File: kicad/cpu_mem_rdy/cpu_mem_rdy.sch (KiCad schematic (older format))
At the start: 37 parts, among them CON1 USB-MICRO-B, P1 CONN_02X04, P3 CONN_01X03, P4 CONN_02X02, P6 POWER, SW1 SW_PUSH, U1 W65C02SP, U2 LM555N, U3 74HCT00, U4 74LS393, U6 28C256, U7 HM62256BLP-7, U8 HM62256BLP-7, X1 OSC

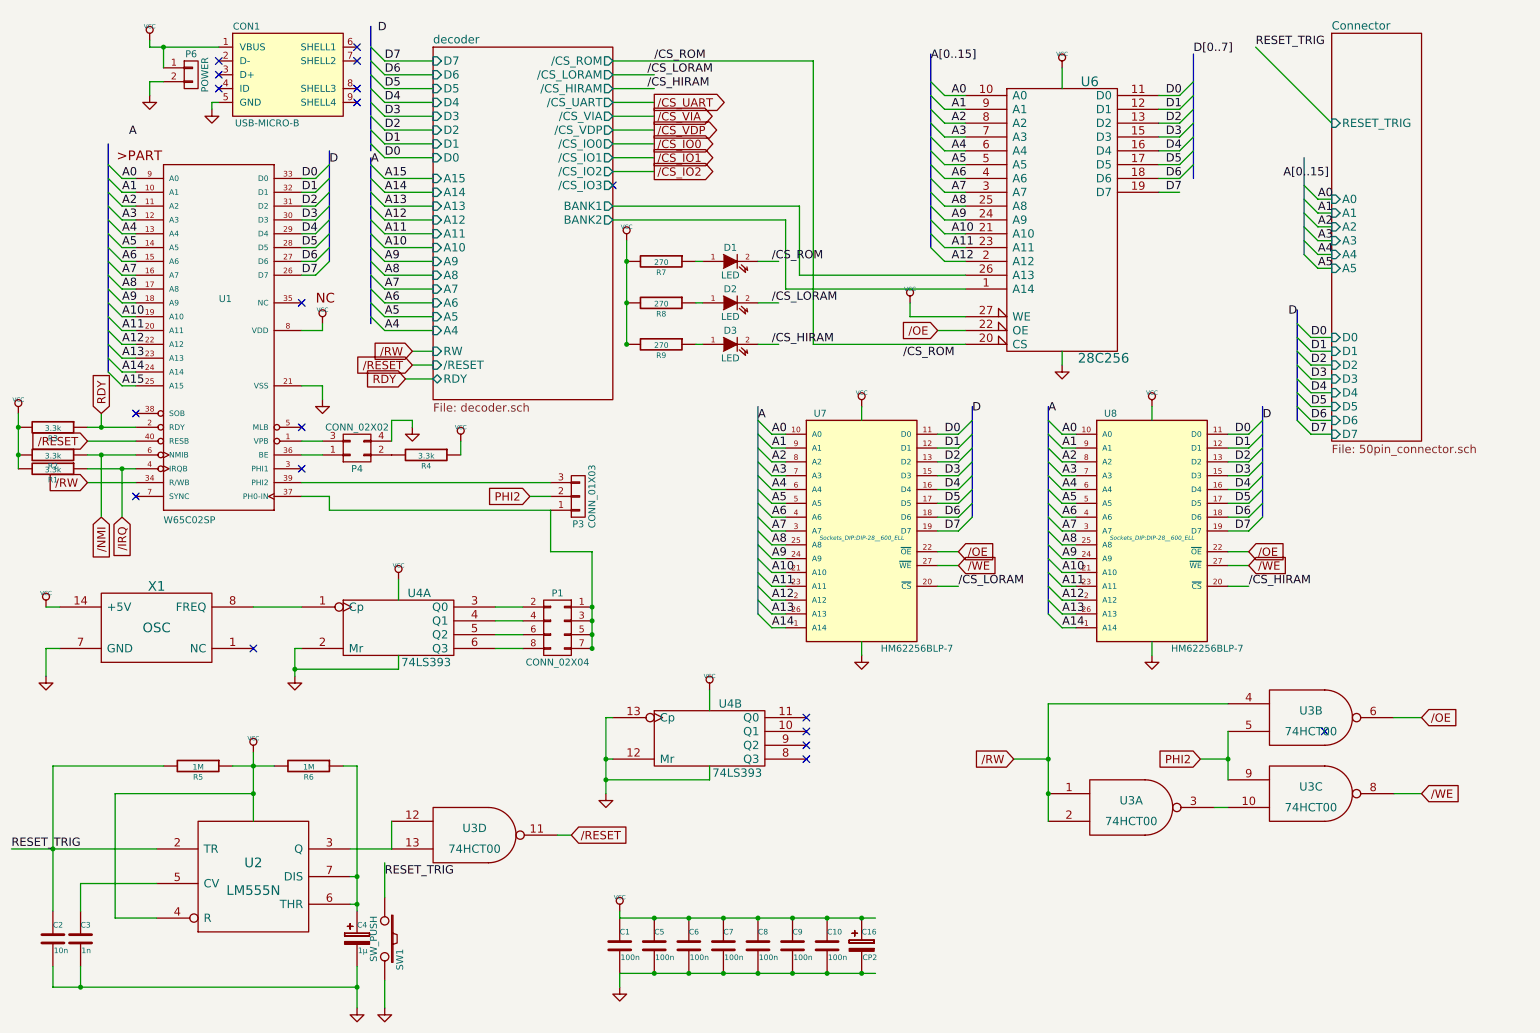
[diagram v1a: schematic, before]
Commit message: no rdy for via, io1-3 connected to rdygen
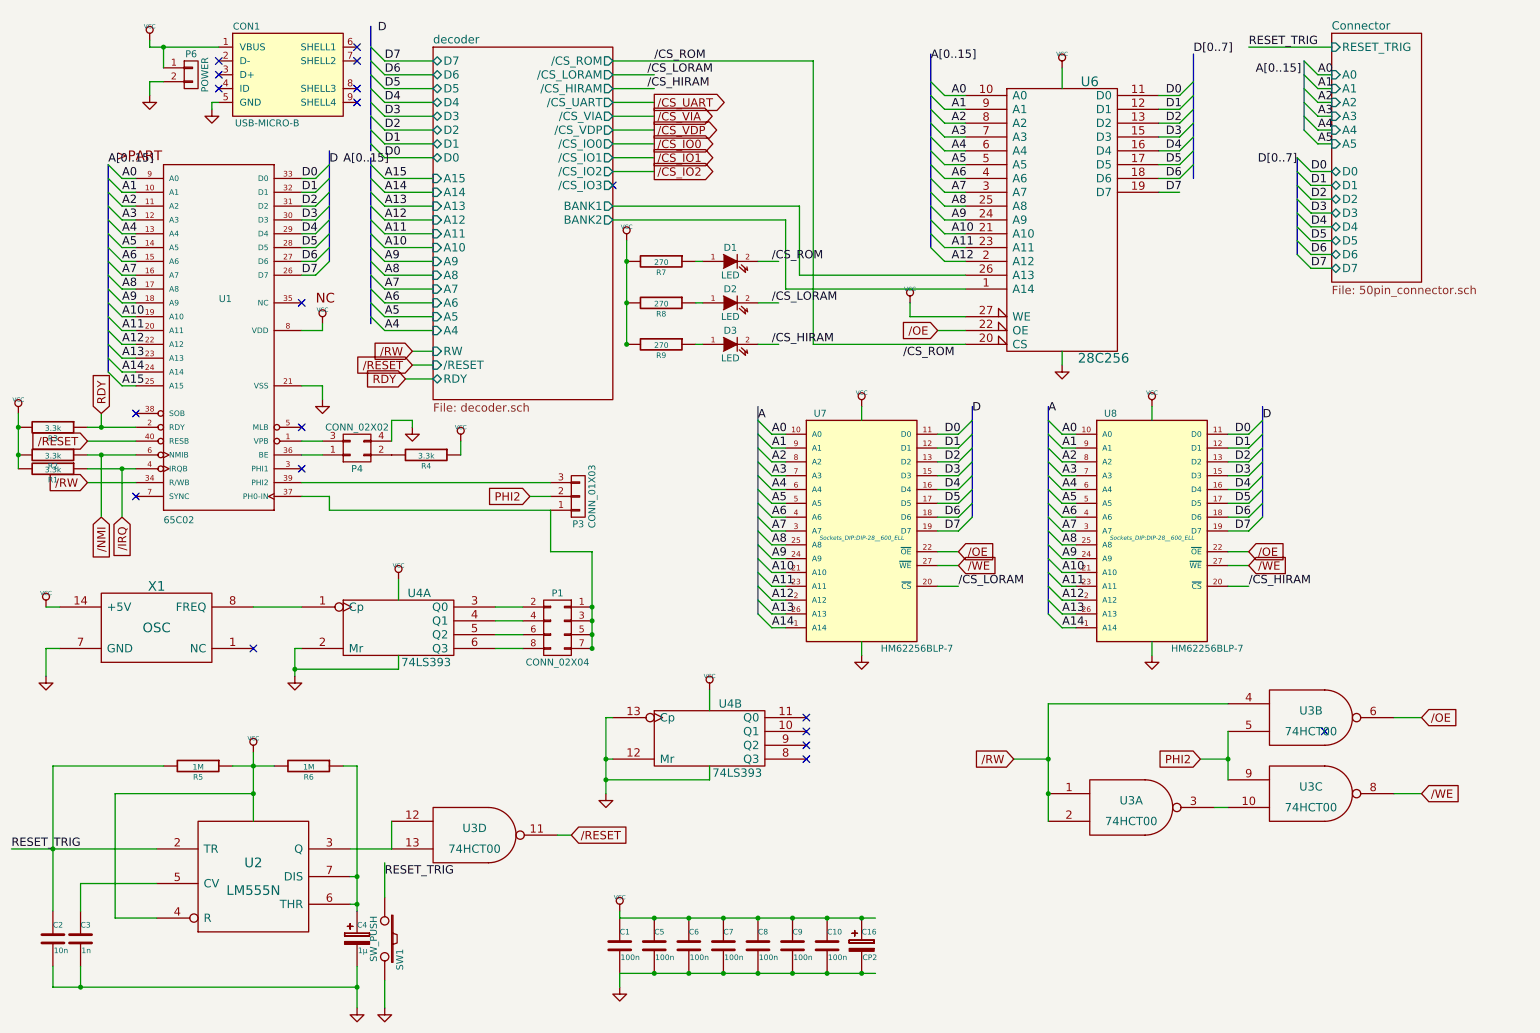
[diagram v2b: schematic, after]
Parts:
- U1: value W65C02SP -> 65C02; footprint Sockets_DIP:DIP-40__600_ELL -> Housings_DIP:DIP-40_W15.24mm_LongPads
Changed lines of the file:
@@
 P 2000 2550
 F 0 "U1" H 2000 2550 50  0000 L BNN
-F 1 "W65C02SP" H 1600 950 50  0000 L BNN
-F 2 "Sockets_DIP:DIP-40__600_ELL" H 2000 2700 50  0001 C CNN
+F 1 "65C02" H 1600 950 50  0000 L BNN
+F 2 "Housings_DIP:DIP-40_W15.24mm_LongPads" H 2000 2700 50  0001 C CNN
 F 3 "" H 2000 2550 60  0000 C CNN
 	1    2000 2550
@@
 Text Label 8000 3350 0    60   ~ 0
 A
-Text Label 1350 1350 0    60   ~ 0
-A
+Text Label 1200 1550 0    60   ~ 0
+A[0..15]
 Text Label 2800 1550 0    60   ~ 0
 D
@@
 $EndComp
 Entry Wire Line
-	9850 1700 9950 1800
-Text Label 9700 1650 0    60   ~ 0
+	9850 800  9950 900
+Text Label 9500 900  0    60   ~ 0
 A[0..15]
-Text Label 9950 1800 0    60   ~ 0
+Text Label 9950 900  0    60   ~ 0
 A0
 Entry Wire Line
-	9850 1800 9950 1900
-Entry Wire Line
-	9850 1900 9950 2000
-Entry Wire Line
-	9850 2000 9950 2100
-Entry Wire Line
-	9850 2100 9950 2200
-Text Label 9950 1900 0    60   ~ 0
+	9850 900  9950 1000
+Entry Wire Line
+	9850 1000 9950 1100
+Entry Wire Line
+	9850 1100 9950 1200
+Entry Wire Line
+	9850 1200 9950 1300
+Text Label 9950 1000 0    60   ~ 0
 A1
-Text Label 9950 2000 0    60   ~ 0
+Text Label 9950 1100 0    60   ~ 0
 A2
-Text Label 9950 2100 0    60   ~ 0
+Text Label 9950 1200 0    60   ~ 0
 A3
-Text Label 9950 2200 0    60   ~ 0
+Text Label 9950 1300 0    60   ~ 0
 A4
 Entry Wire Line
-	9900 2800 9800 2700
-Entry Wire Line
-	9900 2900 9800 2800
-Entry Wire Line
-	9900 3000 9800 2900
-Entry Wire Line
-	9900 3100 9800 3000
-Entry Wire Line
-	9900 3200 9800 3100
-Entry Wire Line
-	9900 3300 9800 3200
-Entry Wire Line
-	9900 3400 9800 3300
-Entry Wire Line
-	9900 3500 9800 3400
-Text Label 9800 2650 2    60   ~ 0
-D
+	9900 1600 9800 1500
+Entry Wire Line
+	9900 1700 9800 1600
+Entry Wire Line
+	9900 1800 9800 1700
+Entry Wire Line
+	9900 1900 9800 1800
+Entry Wire Line
+	9900 2000 9800 1900
+Entry Wire Line
+	9900 2100 9800 2000
+Entry Wire Line
+	9900 2200 9800 2100
+Entry Wire Line
+	9900 2300 9800 2200
+Text Label 9800 1550 2    60   ~ 0
+D[0..7]
 $Comp
 L 28C256 U6
@@
 	1    0    0    -1
 $EndComp
-Text Label 9900 2800 0    60   ~ 0
+Text Label 9900 1600 0    60   ~ 0
 D0
-Text Label 9900 2900 0    60   ~ 0
+Text Label 9900 1700 0    60   ~ 0
 D1
-Text Label 9900 3000 0    60   ~ 0
+Text Label 9900 1800 0    60   ~ 0
 D2
-Text Label 9900 3100 0    60   ~ 0
+Text Label 9900 1900 0    60   ~ 0
 D3
-Text Label 9900 3200 0    60   ~ 0
+Text Label 9900 2000 0    60   ~ 0
 D4
-Text Label 9900 3300 0    60   ~ 0
+Text Label 9900 2100 0    60   ~ 0
 D5
-Text Label 9900 3400 0    60   ~ 0
+Text Label 9900 2200 0    60   ~ 0
 D6
-Text Label 9900 3500 0    60   ~ 0
+Text Label 9900 2300 0    60   ~ 0
 D7
 Text GLabel 1150 4100 3    60   Input ~ 0
@@
 RDY
 Entry Wire Line
-	9850 2200 9950 2300
-Text Label 9950 2300 0    60   ~ 0
+	9850 1300 9950 1400
+Text Label 9950 1400 0    60   ~ 0
 A5
 $Comp
@@
 F1 "decoder.sch" 60
 F2 "A4" I L 3550 2750 60
-F3 "D0" I L 3550 1500 60
-F4 "D1" I L 3550 1400 60
-F5 "D2" I L 3550 1300 60
-F6 "D3" I L 3550 1200 60
-F7 "D4" I L 3550 1100 60
-F8 "D5" I L 3550 1000 60
-F9 "D6" I L 3550 900 60
-F10 "D7" I L 3550 800 60
+F3 "D0" B L 3550 1500 60
+F4 "D1" B L 3550 1400 60
+F5 "D2" B L 3550 1300 60
+F6 "D3" B L 3550 1200 60
+F7 "D4" B L 3550 1100 60
+F8 "D5" B L 3550 1000 60
+F9 "D6" B L 3550 900 60
+F10 "D7" B L 3550 800 60
 F11 "A5" I L 3550 2650 60
 F12 "A6" I L 3550 2550 60
@@
 	3100 1400 3200 1500
 Wire Bus Line
-	1200 1400 1200 3050
+	1200 1550 1200 3050
 Wire Bus Line
 	2800 1450 2800 2250
@@
 	1250 7000 1250 6100
 Wire Wire Line
-	1250 6100 2250 6100
+	2250 6100 1250 6100
 Connection ~ 2250 6100
 Wire Wire Line
@@
 	3400 3400 3400 3450
 Wire Bus Line
-	9850 1500 9850 2200
-Wire Wire Line
-	9950 1800 10050 1800
-Wire Wire Line
-	9950 1900 10050 1900
-Wire Wire Line
-	9950 2000 10050 2000
-Wire Wire Line
-	9950 2100 10050 2100
+	9850 800  9850 1300
+Wire Wire Line
+	9950 900  10050 900
+Wire Wire Line
+	9950 1000 10050 1000
+Wire Wire Line
+	9950 1100 10050 1100
+Wire Wire Line
+	9950 1200 10050 1200
 Wire Bus Line
-	9800 2600 9800 3400
-Wire Wire Line
-	9900 2800 10050 2800
-Wire Wire Line
-	10050 2900 9900 2900
-Wire Wire Line
-	9900 3000 10050 3000
-Wire Wire Line
-	10050 3100 9900 3100
-Wire Wire Line
-	9900 3200 10050 3200
-Wire Wire Line
-	10050 3300 9900 3300
-Wire Wire Line
-	9900 3400 10050 3400
-Wire Wire Line
-	10050 3500 9900 3500
+	9800 1500 9800 2200
+Wire Wire Line
+	9900 1600 10050 1600
+Wire Wire Line
+	10050 1700 9900 1700
+Wire Wire Line
+	9900 1800 10050 1800
+Wire Wire Line
+	10050 1900 9900 1900
+Wire Wire Line
+	9900 2000 10050 2000
+Wire Wire Line
+	10050 2100 9900 2100
+Wire Wire Line
+	9900 2200 10050 2200
+Wire Wire Line
+	10050 2300 9900 2300
 Wire Wire Line
 	1150 4100 1150 3650
@@
 Connection ~ 6650 7400
 Wire Wire Line
-	9950 2200 10050 2200
-Wire Wire Line
-	9950 2300 10050 2300
+	9950 1300 10050 1300
+Wire Wire Line
+	9950 1400 10050 1400
 Wire Wire Line
 	8100 3000 8100 2900
@@
 Wire Wire Line
 	3200 2750 3550 2750
-Text Label 3100 1550 0    60   ~ 0
-A
+Text Label 2900 1550 0    60   ~ 0
+A[0..15]
 Text Label 3200 1650 0    60   ~ 0
 A15
@@
 NoConn ~ 6250 5850
 Wire Wire Line
-	10050 1250 9500 700
-Text Label 9500 700  0    60   ~ 0
+	10050 700  9450 700
+Text Label 9450 700  0    60   ~ 0
 RESET_TRIG
 Text Label 500  6500 0    60   ~ 0
@@
 Wire Wire Line
 	3350 3100 3550 3100
-$Sheet
-S 10050 600  650  2950
-U 54206EE0
-F0 "Connector" 60
-F1 "50pin_connector.sch" 60
-F2 "A0" I L 10050 1800 60
-F3 "A1" I L 10050 1900 60
-F4 "A2" I L 10050 2000 60
-F5 "A3" I L 10050 2100 60
-F6 "A4" I L 10050 2200 60
-F7 "D0" I L 10050 2800 60
-F8 "D1" I L 10050 2900 60
-F9 "D2" I L 10050 3000 60
-F10 "D3" I L 10050 3100 60
-F11 "D4" I L 10050 3200 60
-F12 "D5" I L 10050 3300 60
-F13 "D6" I L 10050 3400 60
-F14 "D7" I L 10050 3500 60
-F15 "A5" I L 10050 2300 60
-F16 "RESET_TRIG" I L 10050 1250 60
-$EndSheet
 $Comp
 L USB-MICRO-B CON1
@@
 Wire Wire Line
 	1500 700  1500 650
+$Sheet
+S 10050 600  650  1800
+U 54206EE0
+F0 "Connector" 60
+F1 "50pin_connector.sch" 60
+F2 "A0" I L 10050 900 60
+F3 "A1" I L 10050 1000 60
+F4 "A2" I L 10050 1100 60
+F5 "A3" I L 10050 1200 60
+F6 "A4" I L 10050 1300 60
+F7 "D0" B L 10050 1600 60
+F8 "D1" B L 10050 1700 60
+F9 "D2" B L 10050 1800 60
+F10 "D3" B L 10050 1900 60
+F11 "D4" B L 10050 2000 60
+F12 "D5" B L 10050 2100 60
+F13 "D6" B L 10050 2200 60
+F14 "D7" B L 10050 2300 60
+F15 "A5" I L 10050 1400 60
+F16 "RESET_TRIG" I L 10050 700 60
+$EndSheet
 $EndSCHEMATC

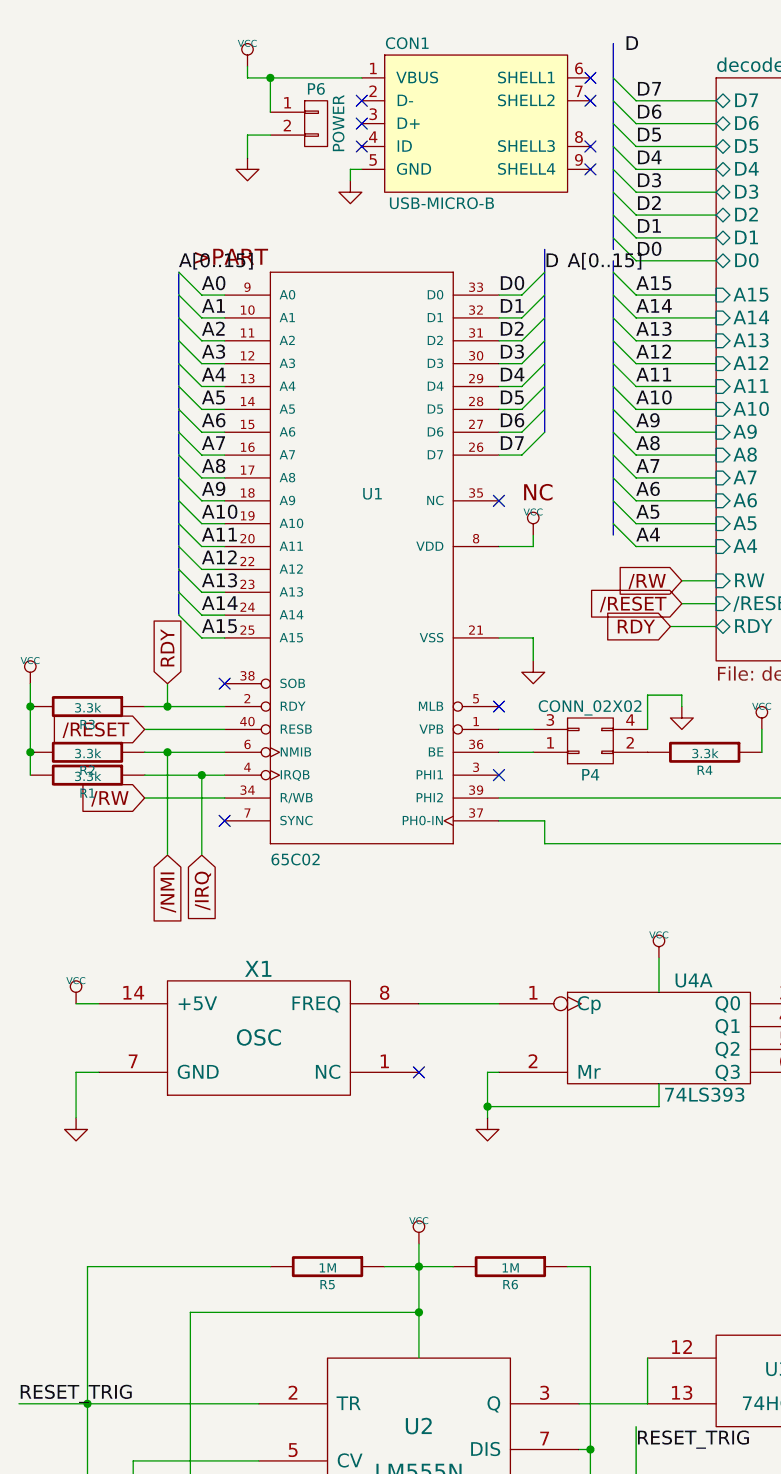
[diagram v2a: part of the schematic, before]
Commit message: USB B for power
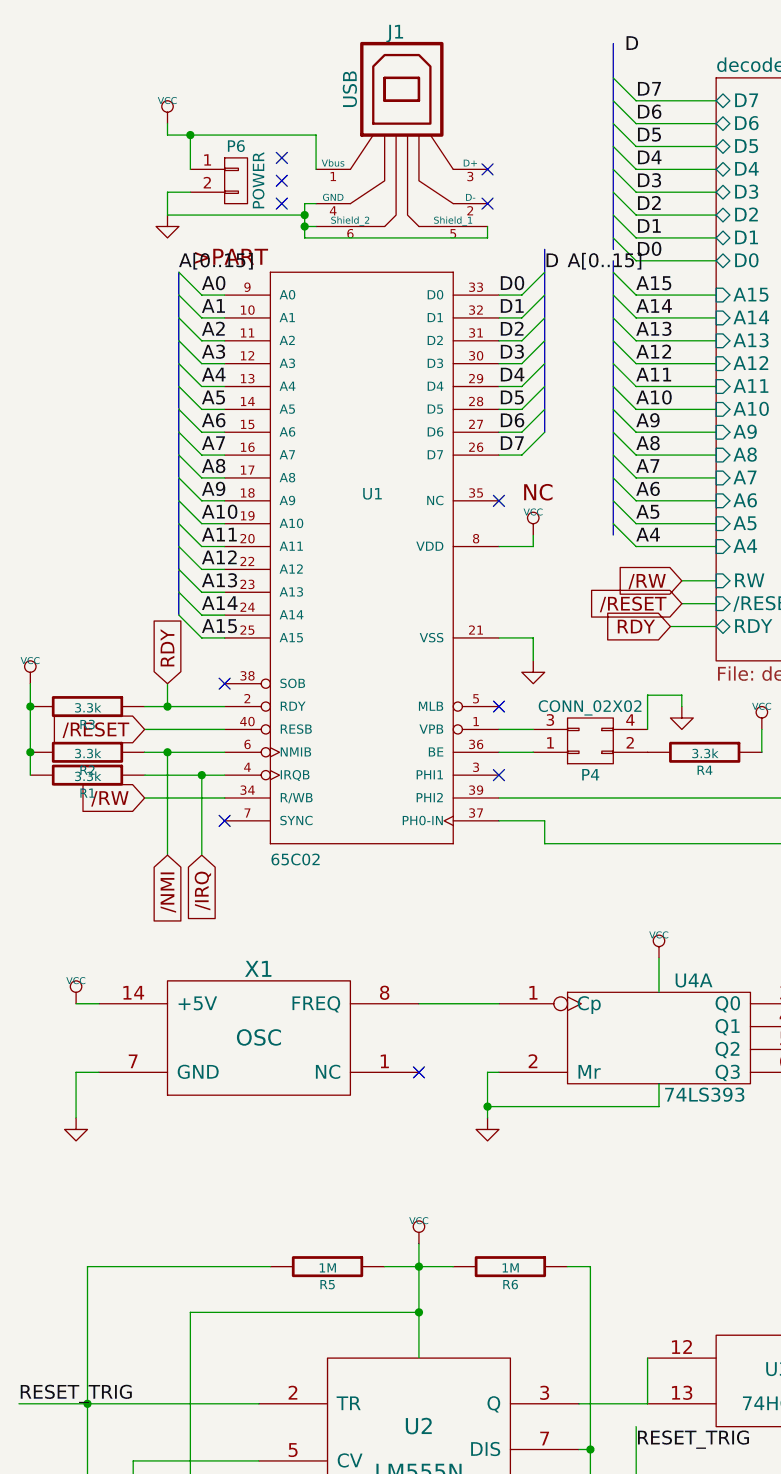
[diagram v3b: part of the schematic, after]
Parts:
- removed CON1: USB-MICRO-B, Connect:USB_Micro-B, symbol USB-MICRO-B
- added J1: USB, Connect:USB_B, symbol USB
- U1: footprint Housings_DIP:DIP-40_W15.24mm_LongPads -> Sockets_DIP:DIP-40__600_ELL
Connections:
- net GND: now also J1.4 (GND), J1.5 (Shield_1), J1.6 (Shield_2)
- net VCC: now also J1.1 (Vbus)
- no-connect marks 19 -> 17
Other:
- moved on the sheet: P6
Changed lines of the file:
@@
 F 0 "U1" H 2000 2550 50  0000 L BNN
 F 1 "65C02" H 1600 950 50  0000 L BNN
-F 2 "Housings_DIP:DIP-40_W15.24mm_LongPads" H 2000 2700 50  0001 C CNN
+F 2 "Sockets_DIP:DIP-40__600_ELL" H 2000 2700 50  0001 C CNN
 F 3 "" H 2000 2550 60  0000 C CNN
 	1    2000 2550
@@
 	1250 7000 1250 6100
 Wire Wire Line
-	2250 6100 1250 6100
+	1250 6100 2250 6100
 Connection ~ 2250 6100
 Wire Wire Line
@@
 L GND #PWR024
 U 1 1 54B5858D
-P 1500 1050
-F 0 "#PWR024" H 1500 1050 30  0001 C CNN
-F 1 "GND" H 1500 980 30  0001 C CNN
-F 2 "" H 1500 1050 60  0000 C CNN
-F 3 "" H 1500 1050 60  0000 C CNN
-	1    1500 1050
-	1    0    0    -1
-$EndComp
-Wire Wire Line
-	1600 950  1500 950
-Wire Wire Line
-	1500 950  1500 1050
+P 1150 1300
+F 0 "#PWR024" H 1150 1300 30  0001 C CNN
+F 1 "GND" H 1150 1230 30  0001 C CNN
+F 2 "" H 1150 1300 60  0000 C CNN
+F 3 "" H 1150 1300 60  0000 C CNN
+	1    1150 1300
+	1    0    0    -1
+$EndComp
+Wire Wire Line
+	1250 1200 1150 1200
+Wire Wire Line
+	1150 1200 1150 1300
 $Comp
 L LED D1
@@
 Wire Wire Line
 	3350 3100 3550 3100
-$Comp
-L USB-MICRO-B CON1
-U 1 1 56B0E071
-P 2500 900
-F 0 "CON1" H 2200 1250 50  0000 C CNN
-F 1 "USB-MICRO-B" H 2350 550 50  0000 C CNN
-F 2 "Connect:USB_Micro-B" H 2500 800 50  0001 C CNN
-F 3 "" H 2500 800 50  0000 C CNN
-	1    2500 900
-	1    0    0    -1
-$EndComp
-$Comp
-L GND #PWR026
-U 1 1 56B0EAD2
-P 1950 1150
-F 0 "#PWR026" H 1950 1150 30  0001 C CNN
-F 1 "GND" H 1950 1080 30  0001 C CNN
-F 2 "" H 1950 1150 60  0000 C CNN
-F 3 "" H 1950 1150 60  0000 C CNN
-	1    1950 1150
-	1    0    0    -1
-$EndComp
-Wire Wire Line
-	1950 1150 1950 1100
-Wire Wire Line
-	1950 1100 2000 1100
-$Comp
-L VCC #PWR027
+Wire Wire Line
+	1750 1250 1800 1250
+$Comp
+L VCC #PWR026
 U 1 1 56B0EDB8
-P 1500 650
-F 0 "#PWR027" H 1500 750 30  0001 C CNN
-F 1 "VCC" H 1500 750 30  0000 C CNN
-F 2 "" H 1500 650 60  0000 C CNN
-F 3 "" H 1500 650 60  0000 C CNN
-	1    1500 650
-	1    0    0    -1
-$EndComp
-NoConn ~ 3000 700
-NoConn ~ 3000 800
-NoConn ~ 3000 1000
-NoConn ~ 3000 1100
-NoConn ~ 2000 800
-NoConn ~ 2000 900
-NoConn ~ 2000 1000
+P 1150 900
+F 0 "#PWR026" H 1150 1000 30  0001 C CNN
+F 1 "VCC" H 1150 1000 30  0000 C CNN
+F 2 "" H 1150 900 60  0000 C CNN
+F 3 "" H 1150 900 60  0000 C CNN
+	1    1150 900
+	1    0    0    -1
+$EndComp
+NoConn ~ 2550 1100
+NoConn ~ 2550 1250
+NoConn ~ 1650 1050
+NoConn ~ 1650 1150
+NoConn ~ 1650 1250
 $Comp
 L CONN_01X02 P6
 U 1 1 56B11104
-P 1800 900
-F 0 "P6" H 1800 1050 50  0000 C CNN
-F 1 "POWER" V 1900 900 50  0000 C CNN
-F 2 "Pin_Headers:Pin_Header_Straight_1x02" H 1800 900 60  0001 C CNN
-F 3 "" H 1800 900 60  0000 C CNN
-	1    1800 900
-	1    0    0    -1
-$EndComp
-Wire Wire Line
-	1600 850  1600 700
-Wire Wire Line
-	1500 700  2000 700
-Connection ~ 1600 700
-Wire Wire Line
-	1500 700  1500 650
+P 1450 1150
+F 0 "P6" H 1450 1300 50  0000 C CNN
+F 1 "POWER" V 1550 1150 50  0000 C CNN
+F 2 "Pin_Headers:Pin_Header_Straight_1x02" H 1450 1150 60  0001 C CNN
+F 3 "" H 1450 1150 60  0000 C CNN
+	1    1450 1150
+	1    0    0    -1
+$EndComp
+Wire Wire Line
+	1250 1100 1250 950
+Wire Wire Line
+	1150 950  1800 950
+Connection ~ 1250 950
+Wire Wire Line
+	1150 950  1150 900
 $Sheet
 S 10050 600  650  1800
@@
 F16 "RESET_TRIG" I L 10050 700 60
 $EndSheet
+$Comp
+L USB J1
+U 1 1 56BB81D0
+P 2200 900
+F 0 "J1" H 2150 1300 60  0000 C CNN
+F 1 "USB" V 1950 1050 60  0000 C CNN
+F 2 "Connect:USB_B" H 2200 900 60  0001 C CNN
+F 3 "" H 2200 900 60  0000 C CNN
+	1    2200 900
+	1    0    0    -1
+$EndComp
+Wire Wire Line
+	2550 1350 2550 1400
+Wire Wire Line
+	2550 1400 1750 1400
+Wire Wire Line
+	1800 1350 1750 1350
+Connection ~ 1750 1350
+Wire Wire Line
+	1750 1400 1750 1250
+Wire Wire Line
+	1150 1300 1750 1300
+Connection ~ 1750 1300
+Wire Wire Line
+	1800 950  1800 1100
 $EndSCHEMATC
